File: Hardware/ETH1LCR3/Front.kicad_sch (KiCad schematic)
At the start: 4 parts, among them J1301 5227161-1, J1302 5227161-1, J1303 5227161-1, J1304 5227161-1

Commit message: Hardware
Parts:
- J1301, J1302, J1303, J1304: footprint (none) -> ETH1LCR3:TE_5227161-1
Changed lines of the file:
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@@
 			)
 		)
-		(property "Footprint" ""
+		(property "Footprint" "ETH1LCR3:TE_5227161-1"
 			(at 133.35 110.49 0)
 			(effects
@@
 			)
 		)
-		(property "Footprint" ""
+		(property "Footprint" "ETH1LCR3:TE_5227161-1"
 			(at 133.35 69.85 0)
 			(effects
@@
 			)
 		)
-		(property "Footprint" ""
+		(property "Footprint" "ETH1LCR3:TE_5227161-1"
 			(at 133.35 90.17 0)
 			(effects
@@
 			)
 		)
-		(property "Footprint" ""
+		(property "Footprint" "ETH1LCR3:TE_5227161-1"
 			(at 133.35 49.53 0)
 			(effects

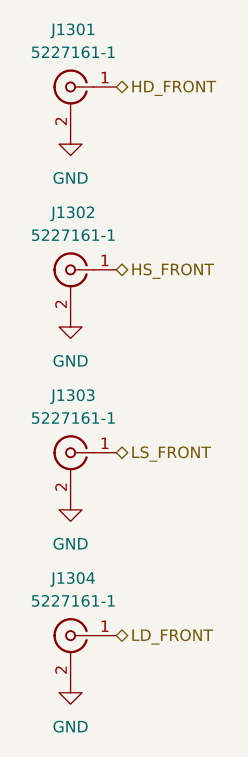
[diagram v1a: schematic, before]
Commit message: Updated project to KiCAD 9
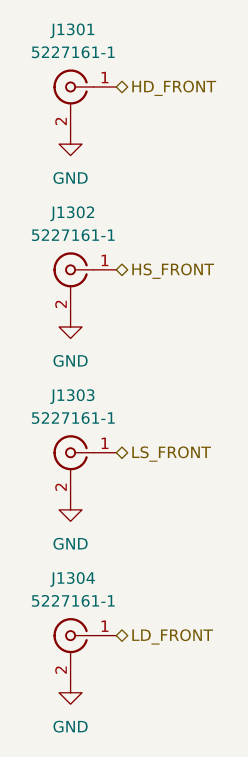
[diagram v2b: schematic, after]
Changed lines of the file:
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@@
 (kicad_sch
-	(version 20231120)
+	(version 20250114)
 	(generator "eeschema")
-	(generator_version "8.0")
+	(generator_version "9.0")
 	(paper "A4")
 	(hierarchical_label "LS_FRONT"
 		(shape bidirectional)
 		(at 138.43 90.17 0)
-		(fields_autoplaced yes)
 		(effects
 			(font
@@
 		(shape bidirectional)
 		(at 138.43 110.49 0)
-		(fields_autoplaced yes)
 		(effects
 			(font
@@
 		(shape bidirectional)
 		(at 138.43 69.85 0)
-		(fields_autoplaced yes)
 		(effects
 			(font
@@
 		(shape bidirectional)
 		(at 138.43 49.53 0)
-		(fields_autoplaced yes)
 		(effects
 			(font
